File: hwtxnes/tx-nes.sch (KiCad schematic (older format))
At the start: 26 parts, among them IC1 ATMEGA328-A, J1 POWER_JACK, P1 nRF, P2 ISP, P3 DIL16, P7 RX, P8 TX, SW1 DPDT, U1 TCR2EF, U2 MCP73832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

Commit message: Holes big enough to fit standard pins.
The 16 pin interconnect going to the main board has holes that don't
really fit a standard 0.1" header pin.  They fit, only barely with too
much force.  The new size matches the TX/RX holes, which fit the pin
comfortably.
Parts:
- P3: footprint (none) -> nesRF TX:NES_PCB_INTERCONNECT
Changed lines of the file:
@@
 F 0 "P3" H 9400 3300 60  0000 C CNN
 F 1 "DIL16" V 9400 2850 50  0000 C CNN
-F 2 "" H 9400 2850 60  0000 C CNN
+F 2 "nesRF TX:NES_PCB_INTERCONNECT" H 9400 2850 60  0001 C CNN
 F 3 "" H 9400 2850 60  0000 C CNN
 	1    9400 2850

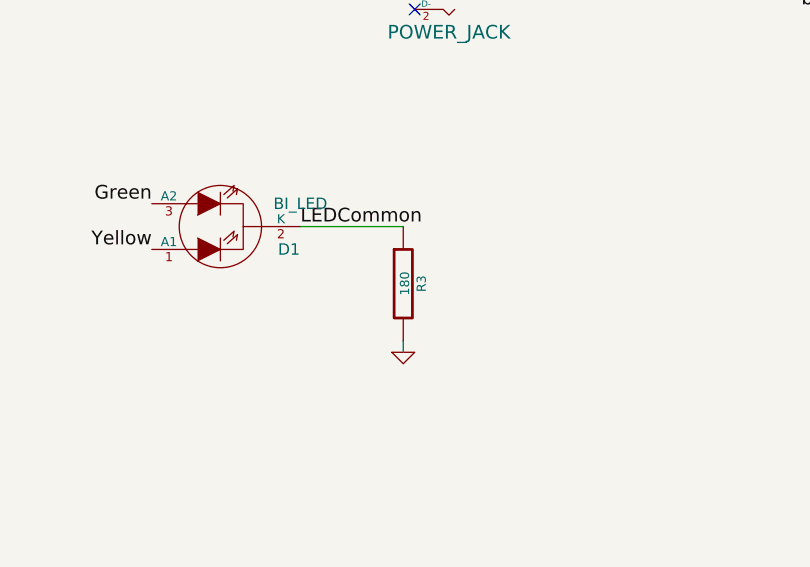
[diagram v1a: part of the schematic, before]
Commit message: Resistor scaled for the WP59GYW bi-color LED.
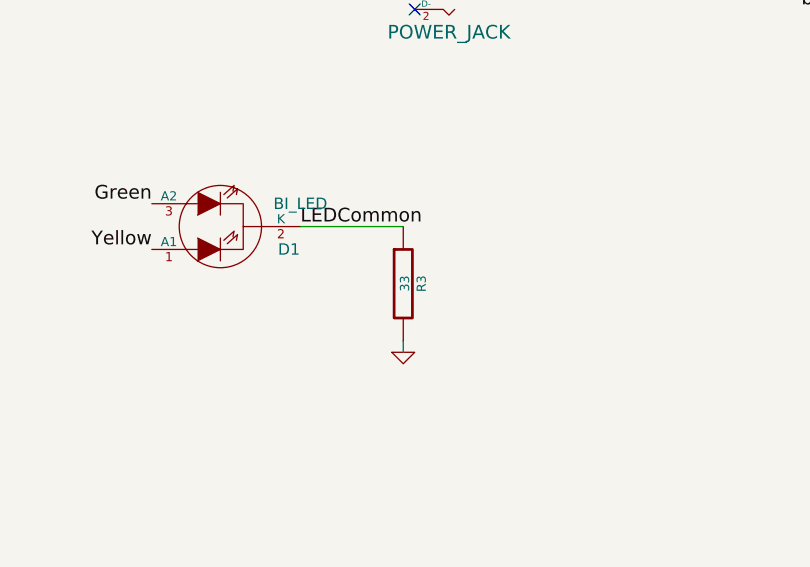
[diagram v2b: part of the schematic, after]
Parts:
- R3: value 180 -> 33
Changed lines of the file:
@@
 P 7200 4400
 F 0 "R3" V 7280 4400 40  0000 C CNN
-F 1 "180" V 7207 4401 40  0000 C CNN
+F 1 "33" V 7207 4401 40  0000 C CNN
 F 2 "Resistors_SMD:R_0402" V 7130 4400 30  0001 C CNN
 F 3 "" H 7200 4400 30  0000 C CNN
